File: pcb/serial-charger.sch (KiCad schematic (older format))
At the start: 12 parts, among them J101 jumper, J102 jumper, P101 USB_OTG, P102 CONN_01X02, P103 CONN_01X04, U101 XC6206

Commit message: reworked bms and mcu to use seeed components
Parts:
- P101: symbol USB_OTG -> USB_OTG-RESCUE-serial-charger
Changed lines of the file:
@@
 EESchema Schematic File Version 2
+LIBS:serial-charger-rescue
 LIBS:power
 LIBS:device
@@
 LIBS:valves
 LIBS:netl
+LIBS:SeeedOPL-Capacitor-2016
+LIBS:SeeedOPL-Connector-2016
+LIBS:SeeedOPL-Crystal Oscillator-2016
+LIBS:SeeedOPL-Diode-2016
+LIBS:SeeedOPL-Display-2016
+LIBS:SeeedOPL-Fuse-2016
+LIBS:SeeedOPL-IC-2016
+LIBS:SeeedOPL-Inductor-2016
+LIBS:SeeedOPL-LED-2016
+LIBS:SeeedOPL-Relay-2016
+LIBS:SeeedOPL-Resistor-2016
+LIBS:SeeedOPL-Sensor-2016
+LIBS:SeeedOPL-Switch-2016
+LIBS:SeeedOPL-Transistor-2016
 LIBS:serial-charger-cache
 EELAYER 25 0
@@
 $EndDescr
 $Comp
-L USB_OTG P101
+L USB_OTG-RESCUE-serial-charger P101
 U 1 1 55AEBD84
 P 1900 2900

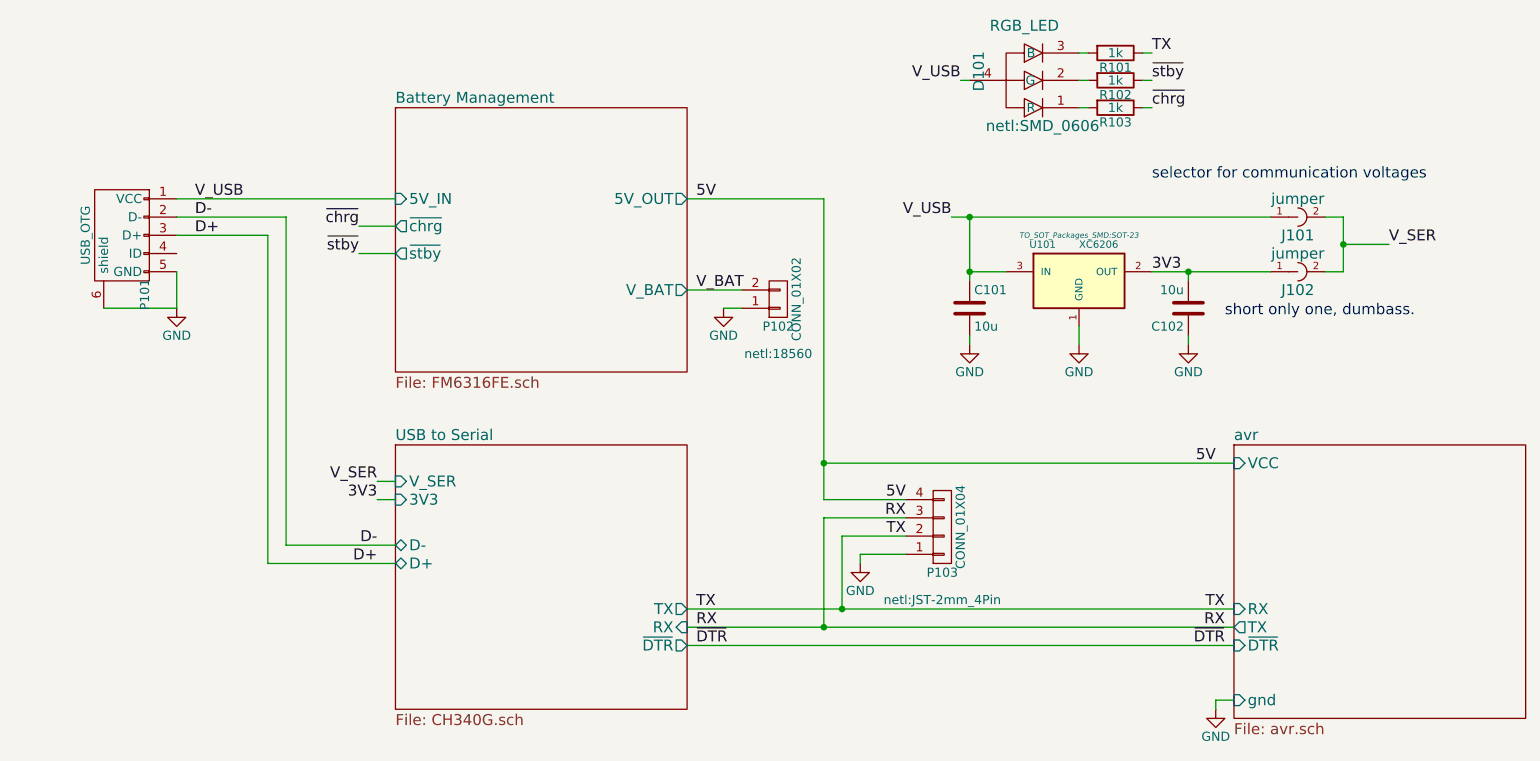
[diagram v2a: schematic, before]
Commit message: finished swapping parts, started layout
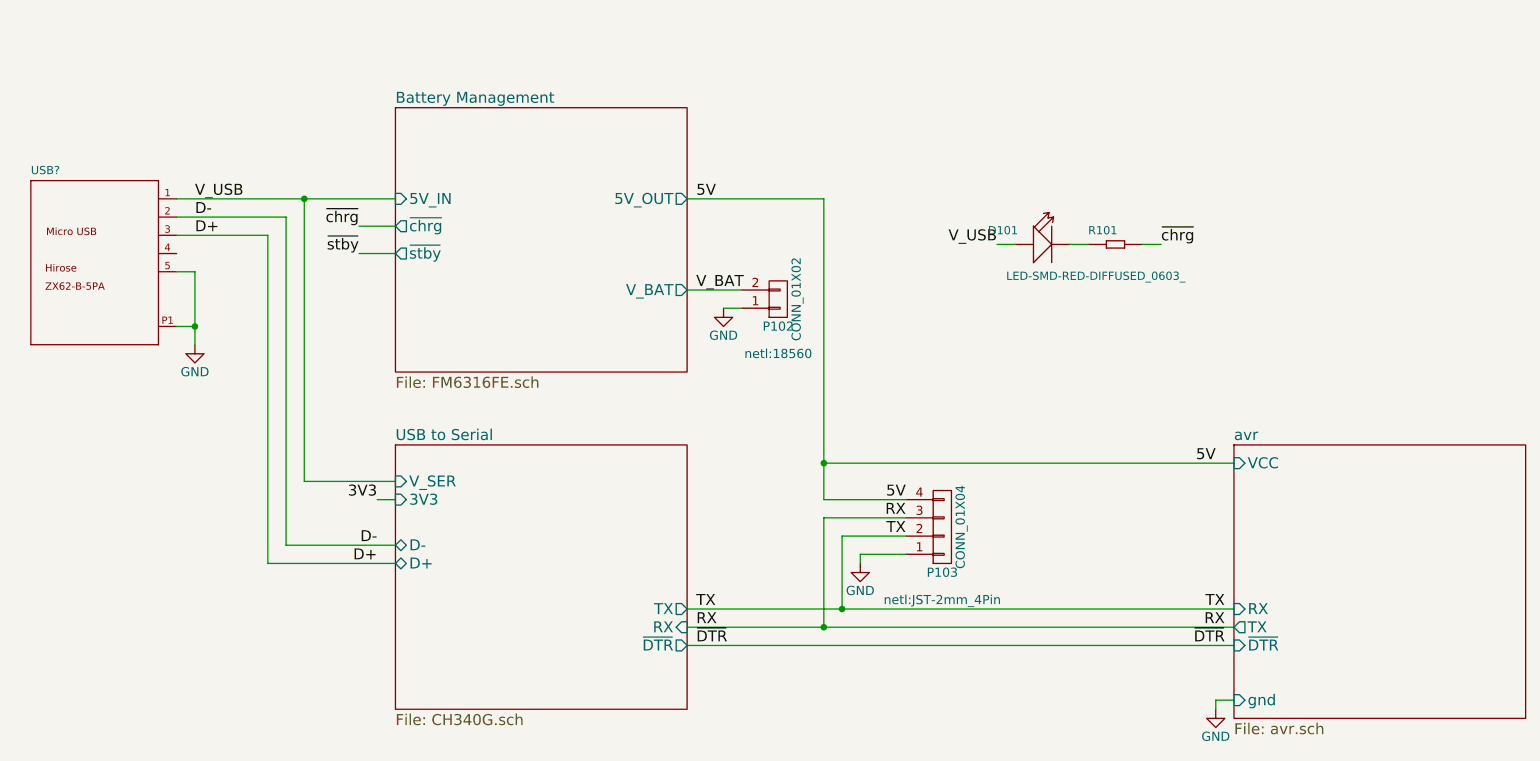
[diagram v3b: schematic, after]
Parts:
- removed C101, C102: 10u, netl:SMD_0603, symbol C
- removed D101: RGB_LED, netl:SMD_0606, symbol RGB_LED
- removed J101, J102: jumper, netl:Jumper, symbol jumper
- removed P101: USB_OTG, Connect:USB_Micro-B, symbol USB_OTG-RESCUE-serial-charger
- removed R101, R102, R103: 1k, netl:SMD_0603, symbol R
- removed U101: XC6206, TO_SOT_Packages_SMD:SOT-23, symbol XC6206
- added D101: LED-SMD-RED-DIFFUSED_0603_, SeeedOPL-LED-2016:LED-0603, symbol LED-SMD-RED-DIFFUSED_0603_
- added R101: SMD-RES-1K-5%-1_10W_0603_, SeeedOPL-Resistor-2016:R0603, symbol SMD-RES-1K-5%-1_10W_0603_
- added USB?: MICRO-USB-SMD_ZX62-B-5PA_, SeeedOPL-Connector-2016:MICRO-USB5+4P-SMD-0.65-B, symbol MICRO-USB-SMD_ZX62-B-5PA_
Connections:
- net D+: now also USB?.3 (D+)
- net D-: now also USB?.2 (D-)
- net GND: now also USB?.5 (GND), USB?.P1 (SHIELD), USB?.P2 (SHIELD), USB?.P3 (SHIELD), USB?.P4 (SHIELD), USB?.P5 (SHIELD), USB?.P6 (SHIELD)
- net V_USB: now also D101.+, USB?.1 (VBUS)
- net ~chrg: now also R101.2
- new net: D101.-, R101.1
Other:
- note removed: "selector for communication voltages"
- note removed: "short only one, dumbass."

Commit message: layout mostly done
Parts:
- gave numbers to parts that had none: 1
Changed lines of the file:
@@
 $EndDescr
 $Comp
-L GND #PWR01
+L GND #PWR101
 U 1 1 55AEBF75
 P 2300 3500
-F 0 "#PWR01" H 2300 3250 50  0001 C CNN
+F 0 "#PWR101" H 2300 3250 50  0001 C CNN
 F 1 "GND" H 2300 3350 50  0000 C CNN
 F 2 "" H 2300 3500 60  0000 C CNN
@@
 	2200 2800 2800 2800
 $Comp
-L GND #PWR02
+L GND #PWR102
 U 1 1 57F8F41D
 P 5200 3300
-F 0 "#PWR02" H 5200 3050 50  0001 C CNN
+F 0 "#PWR102" H 5200 3050 50  0001 C CNN
 F 1 "GND" H 5200 3150 50  0000 C CNN
 F 2 "" H 5200 3300 60  0000 C CNN
@@
 $EndSheet
 $Comp
-L GND #PWR03
+L GND #PWR104
 U 1 1 58B9EA67
 P 7900 5500
-F 0 "#PWR03" H 7900 5250 50  0001 C CNN
+F 0 "#PWR104" H 7900 5250 50  0001 C CNN
 F 1 "GND" H 7900 5350 50  0000 C CNN
 F 2 "" H 7900 5500 50  0000 C CNN
@@
 	5850 4950 5850 4550
 $Comp
-L GND #PWR04
+L GND #PWR103
 U 1 1 58BACB26
 P 5950 4700
-F 0 "#PWR04" H 5950 4450 50  0001 C CNN
+F 0 "#PWR103" H 5950 4450 50  0001 C CNN
 F 1 "GND" H 5950 4550 50  0000 C CNN
 F 2 "" H 5950 4700 50  0000 C CNN
@@
 	6800 2950 6700 2950
 $Comp
-L MICRO-USB-SMD_ZX62-B-5PA_ USB?
+L MICRO-USB-SMD_ZX62-B-5PA_ USB101
 U 1 1 5A559483
 P 1800 3100
-F 0 "USB?" H 1400 3630 45  0000 L BNN
+F 0 "USB101" H 1400 3630 45  0000 L BNN
 F 1 "MICRO-USB-SMD_ZX62-B-5PA_" H 1800 3100 45  0001 L BNN
 F 2 "SeeedOPL-Connector-2016:MICRO-USB5+4P-SMD-0.65-B" H 1800 3100 60  0001 C CNN

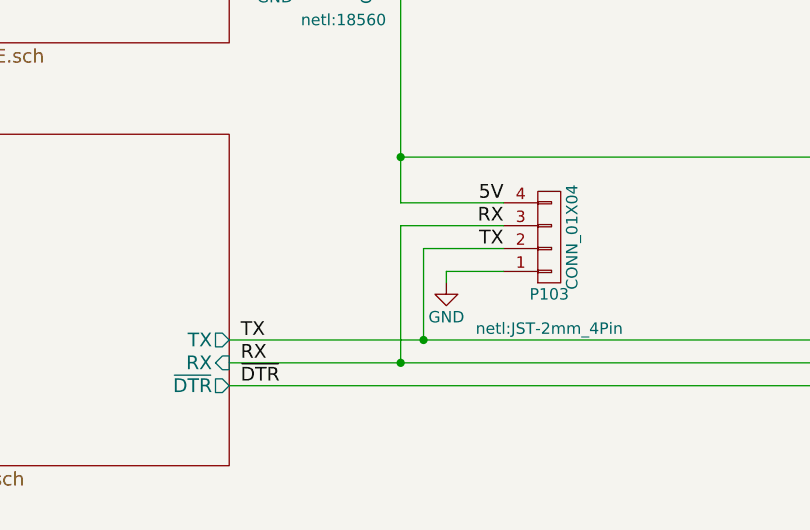
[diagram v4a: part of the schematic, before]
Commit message: added button, capacitor to led strip power and jumpers to external rx/tx. everything layed out and connected
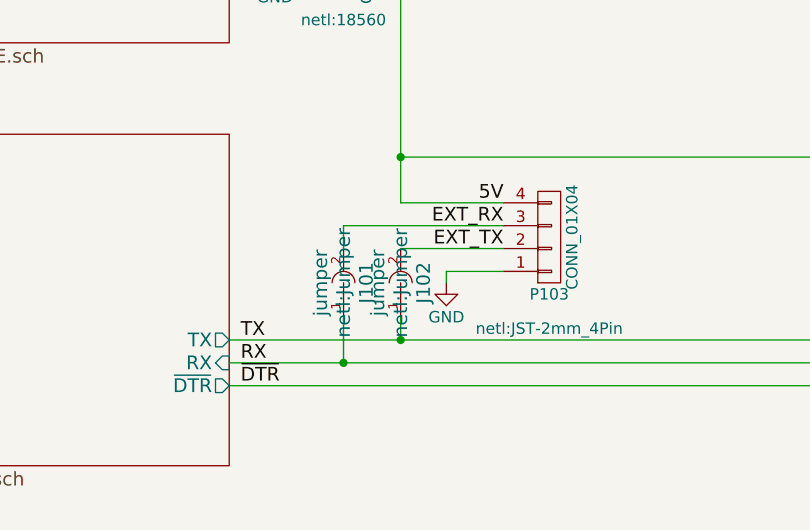
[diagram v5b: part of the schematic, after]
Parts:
- added J101, J102: jumper, netl:Jumper, symbol jumper
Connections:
- net RX: now also J101.1; no longer P103.3 (P3)
- net TX: now also J102.1; no longer P103.2 (P2)
- new net EXT_RX: J101.2, P103.3 (P3)
- new net EXT_TX: J102.2, P103.2 (P2)
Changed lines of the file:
@@
 $EndDescr
 $Comp
-L GND #PWR101
+L GND #PWR01
 U 1 1 55AEBF75
 P 2300 3500
-F 0 "#PWR101" H 2300 3250 50  0001 C CNN
+F 0 "#PWR01" H 2300 3250 50  0001 C CNN
 F 1 "GND" H 2300 3350 50  0000 C CNN
 F 2 "" H 2300 3500 60  0000 C CNN
@@
 	2200 2800 2800 2800
 $Comp
-L GND #PWR102
+L GND #PWR02
 U 1 1 57F8F41D
 P 5200 3300
-F 0 "#PWR102" H 5200 3050 50  0001 C CNN
+F 0 "#PWR02" H 5200 3050 50  0001 C CNN
 F 1 "GND" H 5200 3150 50  0000 C CNN
 F 2 "" H 5200 3300 60  0000 C CNN
@@
 $EndSheet
 $Comp
-L GND #PWR104
+L GND #PWR03
 U 1 1 58B9EA67
 P 7900 5500
-F 0 "#PWR104" H 7900 5250 50  0001 C CNN
+F 0 "#PWR03" H 7900 5250 50  0001 C CNN
 F 1 "GND" H 7900 5350 50  0000 C CNN
 F 2 "" H 7900 5500 50  0000 C CNN
@@
 Text Label 6200 4350 2    60   ~ 0
 5V
-Text Label 6200 4450 2    60   ~ 0
-RX
-Text Label 6200 4550 2    60   ~ 0
-TX
 Text Label 5050 5050 0    60   ~ 0
 RX
@@
 Wire Wire Line
 	5000 4950 8000 4950
-Wire Wire Line
-	5750 4450 6200 4450
-Wire Wire Line
-	5850 4550 6200 4550
 Connection ~ 5750 4150
 Wire Wire Line
@@
 Wire Wire Line
 	5000 2700 5750 2700
-Connection ~ 5850 4950
-Connection ~ 5750 5050
-Wire Wire Line
-	5750 4450 5750 5050
-Wire Wire Line
-	5850 4950 5850 4550
-$Comp
-L GND #PWR103
+$Comp
+L GND #PWR04
 U 1 1 58BACB26
 P 5950 4700
-F 0 "#PWR103" H 5950 4450 50  0001 C CNN
+F 0 "#PWR04" H 5950 4450 50  0001 C CNN
 F 1 "GND" H 5950 4550 50  0000 C CNN
 F 2 "" H 5950 4700 50  0000 C CNN
@@
 	2200 3100 2300 3100
 Connection ~ 2300 3400
+$Comp
+L jumper J101
+U 1 1 5A78C194
+P 5500 4700
+F 0 "J101" H 5500 4600 60  0000 C CNN
+F 1 "jumper" H 5500 4800 60  0000 C CNN
+F 2 "netl:Jumper" H 5500 4700 60  0000 C CNN
+F 3 "" H 5500 4700 60  0000 C CNN
+	1    5500 4700
+	0    -1   -1   0
+$EndComp
+$Comp
+L jumper J102
+U 1 1 5A78C560
+P 5750 4700
+F 0 "J102" H 5750 4600 60  0000 C CNN
+F 1 "jumper" H 5750 4800 60  0000 C CNN
+F 2 "netl:Jumper" H 5750 4700 60  0000 C CNN
+F 3 "" H 5750 4700 60  0000 C CNN
+	1    5750 4700
+	0    -1   -1   0
+$EndComp
+Wire Wire Line
+	5500 4850 5500 5050
+Connection ~ 5500 5050
+Wire Wire Line
+	5500 4550 5500 4450
+Wire Wire Line
+	5750 4850 5750 4950
+Connection ~ 5750 4950
+Wire Wire Line
+	5500 4450 6200 4450
+Wire Wire Line
+	6200 4550 5750 4550
+Text Label 6200 4550 2    60   ~ 0
+EXT_TX
+Text Label 6200 4450 2    60   ~ 0
+EXT_RX
 $EndSCHEMATC
